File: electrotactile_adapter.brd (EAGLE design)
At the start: 28.6 x 12.8 mm, 18 parts, among them J3 PAD_SMD_L0.5_W1, J4 PAD_SMD_L0.5_W1, J5 PAD_SMD_L0.5_W1, J6 PAD_SMD_L0.5_W1, J7 1x33 Molex Connector, J8 1x33 Molex Connector

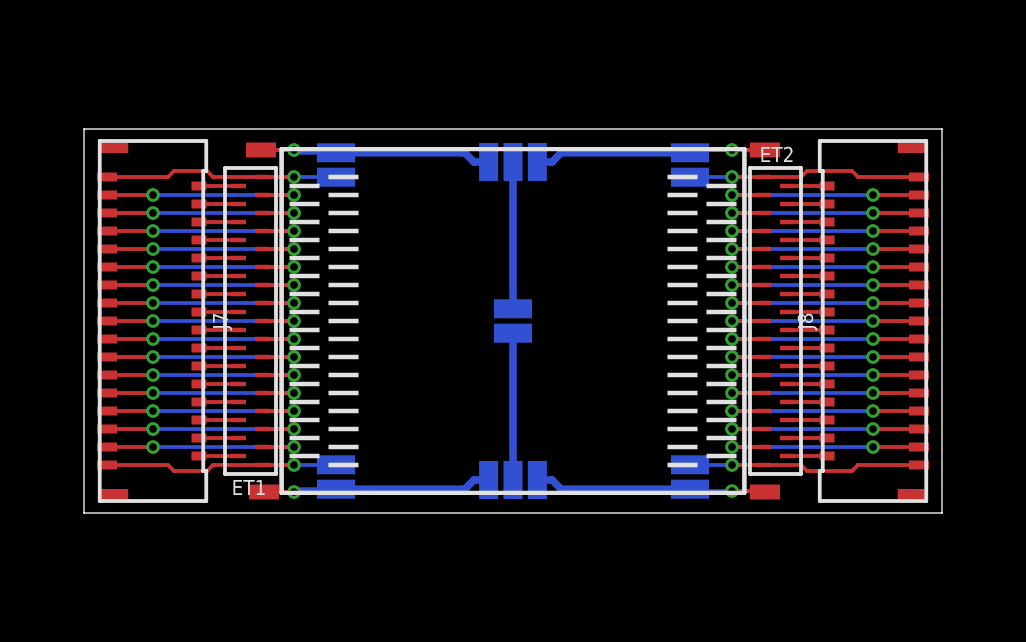
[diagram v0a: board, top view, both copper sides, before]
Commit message: Rev 2.  Need to change size of ET cutout to 16mm x 12mm.
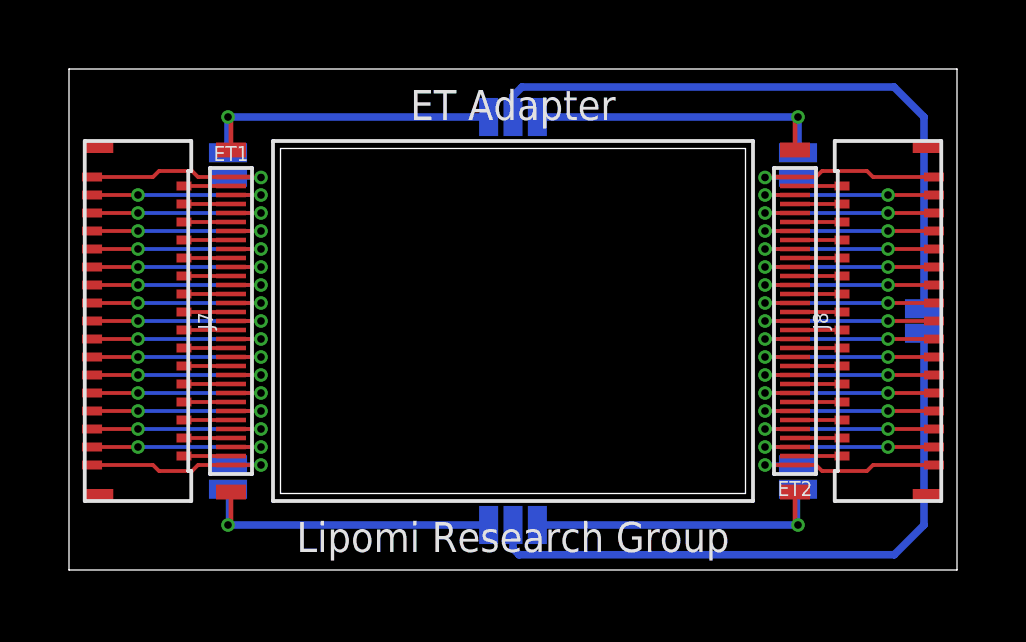
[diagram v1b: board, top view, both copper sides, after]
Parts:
- removed U$1: (no value), PiB_logo:LRG-LOGO
- removed U$6: (no value), lipomi:ELECTOTACTILE_ARRAY_MASK
- ET1, ET2: value ELECTROTACTILE_ARRAY -> ELECTROTACTILE_ARRAY_BONDING_PADS; device lipomi:LIPOMI_ET_ARRAY_CONNECTOR -> lipomi:ELECTROTACTILE_ARRAY_BONDING_PADS
- U$2: device lipomi:ELECTOTACTILE_ARRAY_MASK -> lipomi:ELECTROTACTILE_SUBSTRATE
- moved JP7 13.7 mm to (13.7, 0.00)
- moved JP2 3.60 mm to (-9.50, -5.20)
- moved JP3 3.60 mm to (-9.50, 5.20)
- moved JP4 3.60 mm to (9.50, 5.20)
- moved JP5 3.60 mm to (9.50, -5.20)
- moved JP1 1.50 mm to (0.00, 6.80)
- moved JP6 1.50 mm to (0.00, -6.80)
- moved J4 1.10 mm to (-9.40, -5.70)
- moved J3 1.00 mm to (-9.40, 5.70)
- moved J5 1.00 mm to (9.40, 5.70)
- moved J6 1.00 mm to (9.40, -5.70)
- moved ET1 0.60 mm to (-9.40, 0.00)
- moved ET2 0.60 mm to (9.40, 0.00)
- moved J7 0.50 mm to (-12.5, 0.00)
- moved J8 0.50 mm to (12.5, 0.00)
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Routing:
- net N$71: track 4.89 -> 21.4 mm
- net N$72: track 4.89 -> 21.3 mm
- net N$70: track 7.65 -> 11.0 mm
- net N$69: track 7.75 -> 11.0 mm
- net N$68: track 7.75 -> 11.0 mm
- net N$34: track 7.75 -> 11.0 mm
- net N$48: track 7.80 -> 6.90 mm
- net N$33: track 7.80 -> 6.90 mm
- net N$67: track 7.80 -> 6.91 mm
- net N$14: track 7.80 -> 6.91 mm
- net N$99: track 7.28 -> 6.63 mm
- net N$9: track 7.28 -> 6.63 mm
- net N$7: track 7.28 -> 6.63 mm
- net N$65: track 7.28 -> 6.63 mm
- net N$63: track 7.28 -> 6.63 mm
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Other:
- board size 28.6 x 12.8 mm -> 29.6 x 16.7 mm
- board text added: "Lipomi Research Group"
- board text added: "Rev 2"

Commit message: update for Mickey.
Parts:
- moved J7 0.30 mm to (-12.8, 0.00)
- moved J8 0.30 mm to (12.8, 0.00)
- moved JP2 0.30 mm to (-9.80, -5.20)
- moved JP3 0.30 mm to (-9.80, 5.20)
- moved JP4 0.30 mm to (9.80, 5.20)
- moved JP5 0.30 mm to (9.80, -5.20)
- moved JP7 0.30 mm to (14.0, 0.00)
- moved JP1 0.30 mm to (0.00, 7.10)
- moved JP6 0.30 mm to (0.00, -7.10)
- moved ET1 0.30 mm to (-9.70, 0.00)
- moved ET2 0.30 mm to (9.70, 0.00)
- moved J3 0.30 mm to (-9.70, 5.70)
- moved J4 0.30 mm to (-9.70, -5.70)
- moved J5 0.30 mm to (9.70, 5.70)
- moved J6 0.30 mm to (9.70, -5.70)
- renumbered U$2 to U$1
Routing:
- net N$70: track 11.0 -> 11.9 mm
- net N$69: track 11.0 -> 11.9 mm
- net N$68: track 11.0 -> 11.9 mm
- net N$34: track 11.0 -> 11.9 mm
- net N$71: track 21.4 -> 22.0 mm
- net N$72: track 21.3 -> 21.9 mm
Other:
- board size 29.6 x 16.7 mm -> 30.2 x 17.4 mm
